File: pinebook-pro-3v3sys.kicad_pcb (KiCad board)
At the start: 2 copper layers, 7.8 x 17.9 mm, 23 parts, among them J1 Conn_01x03, J2 Conn_02x03_Counter_Clockwise, J3 Conn_01x01, J4 Conn_01x03, J5 Conn_01x01, U1 TPS63806

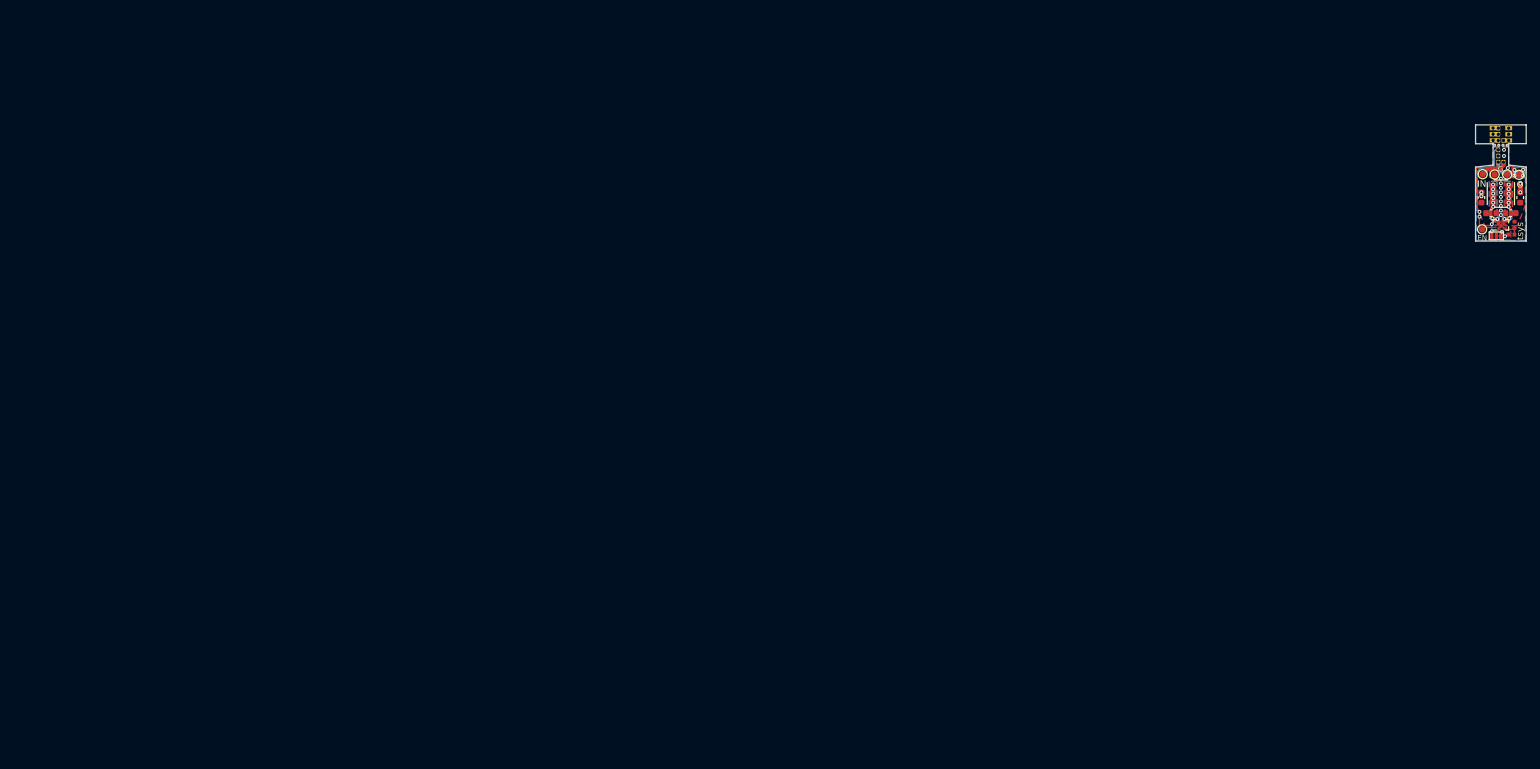
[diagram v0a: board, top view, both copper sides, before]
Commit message: Add manually panelized boards
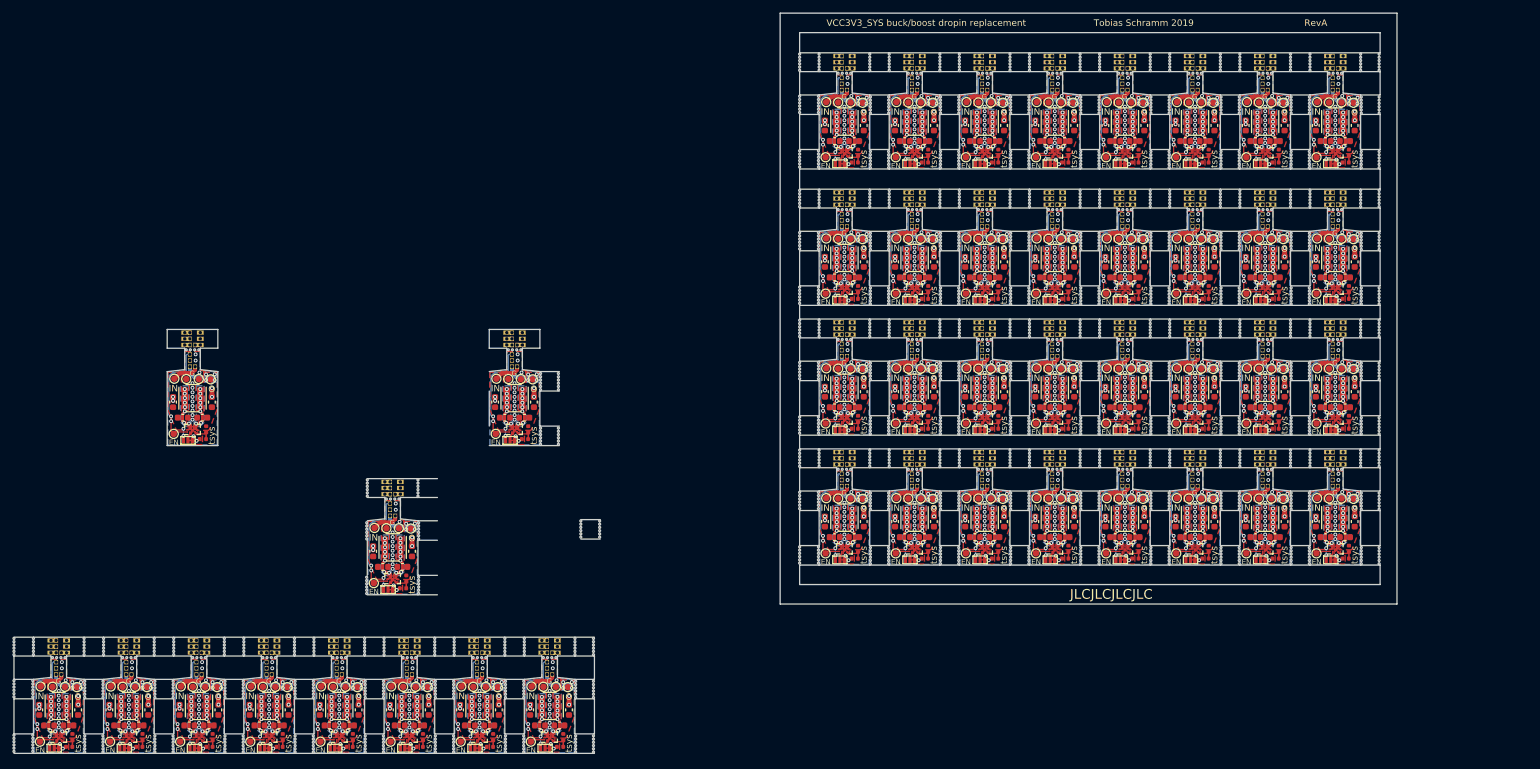
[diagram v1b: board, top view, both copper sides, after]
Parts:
- added C1: 22 uC, Capacitor_SMD:C_0603_1608Metric, F.Cu at (-42.7, 111.9)
- added C1: 22 uC, Capacitor_SMD:C_0603_1608Metric, F.Cu at (-61.7, 136.3)
- added C1: 22 uC, Capacitor_SMD:C_0603_1608Metric, F.Cu at (-29.3, 136.3)
- added C1: 22 uC, Capacitor_SMD:C_0603_1608Metric, F.Cu at (48.5, 46.3)
- added C1: 22 uC, Capacitor_SMD:C_0603_1608Metric, F.Cu at (102.5, 46.3)
- added C1: 22 uC, Capacitor_SMD:C_0603_1608Metric, F.Cu at (59.3, 46.3)
- added C1: 22 uC, Capacitor_SMD:C_0603_1608Metric, F.Cu at (91.7, 46.3)
- added C1: 22 uC, Capacitor_SMD:C_0603_1608Metric, F.Cu at (70.1, 46.3)
- added C1: 22 uC, Capacitor_SMD:C_0603_1608Metric, F.Cu at (80.9, 46.3)
- added C1: 22 uC, Capacitor_SMD:C_0603_1608Metric, F.Cu at (26.9, 46.3)
- added C1: 22 uC, Capacitor_SMD:C_0603_1608Metric, F.Cu at (37.7, 46.3)
- added C1: 22 uC, Capacitor_SMD:C_0603_1608Metric, F.Cu at (-23.9, 88.9)
- added C1: 22 uC, Capacitor_SMD:C_0603_1608Metric, F.Cu at (48.5, 67.3)
- added C1: 22 uC, Capacitor_SMD:C_0603_1608Metric, F.Cu at (102.5, 67.3)
- added C1: 22 uC, Capacitor_SMD:C_0603_1608Metric, F.Cu at (59.3, 67.3)
- added C1: 22 uC, Capacitor_SMD:C_0603_1608Metric, F.Cu at (91.7, 67.3)
- added C1: 22 uC, Capacitor_SMD:C_0603_1608Metric, F.Cu at (70.1, 67.3)
- added C1: 22 uC, Capacitor_SMD:C_0603_1608Metric, F.Cu at (80.9, 67.3)
- added C1: 22 uC, Capacitor_SMD:C_0603_1608Metric, F.Cu at (26.9, 67.3)
- added C1: 22 uC, Capacitor_SMD:C_0603_1608Metric, F.Cu at (37.7, 67.3)
- added C1: 22 uC, Capacitor_SMD:C_0603_1608Metric, F.Cu at (48.5, 87.3)
- added C1: 22 uC, Capacitor_SMD:C_0603_1608Metric, F.Cu at (102.5, 87.3)
- added C1: 22 uC, Capacitor_SMD:C_0603_1608Metric, F.Cu at (59.3, 87.3)
- added C1: 22 uC, Capacitor_SMD:C_0603_1608Metric, F.Cu at (91.7, 87.3)
- added C1: 22 uC, Capacitor_SMD:C_0603_1608Metric, F.Cu at (70.1, 87.3)
- added C1: 22 uC, Capacitor_SMD:C_0603_1608Metric, F.Cu at (80.9, 87.3)
- added C1: 22 uC, Capacitor_SMD:C_0603_1608Metric, F.Cu at (26.9, 87.3)
- added C1: 22 uC, Capacitor_SMD:C_0603_1608Metric, F.Cu at (37.7, 87.3)
- added C1: 22 uC, Capacitor_SMD:C_0603_1608Metric, F.Cu at (102.5, 107.3)
- added C1: 22 uC, Capacitor_SMD:C_0603_1608Metric, F.Cu at (91.7, 107.3)
- added C1: 22 uC, Capacitor_SMD:C_0603_1608Metric, F.Cu at (80.9, 107.3)
- added C1: 22 uC, Capacitor_SMD:C_0603_1608Metric, F.Cu at (70.1, 107.3)
- added C1: 22 uC, Capacitor_SMD:C_0603_1608Metric, F.Cu at (-40.1, 136.3)
- added C1: 22 uC, Capacitor_SMD:C_0603_1608Metric, F.Cu at (59.3, 107.3)
- added C1: 22 uC, Capacitor_SMD:C_0603_1608Metric, F.Cu at (48.5, 107.3)
- added C1: 22 uC, Capacitor_SMD:C_0603_1608Metric, F.Cu at (37.7, 107.3)
- added C1: 22 uC, Capacitor_SMD:C_0603_1608Metric, F.Cu at (26.9, 107.3)
- added C1: 22 uC, Capacitor_SMD:C_0603_1608Metric, F.Cu at (-94.1, 136.3)
- added C1: 22 uC, Capacitor_SMD:C_0603_1608Metric, F.Cu at (-50.9, 136.3)
- added C1: 22 uC, Capacitor_SMD:C_0603_1608Metric, F.Cu at (-18.5, 136.3)
- added C1: 22 uC, Capacitor_SMD:C_0603_1608Metric, F.Cu at (-83.3, 136.3)
- added C1: 22 uC, Capacitor_SMD:C_0603_1608Metric, F.Cu at (-72.5, 136.3)
- added C2: 22 uC, Capacitor_SMD:C_0603_1608Metric, F.Cu at (-17.0, 138.7)
- added C2: 22 uC, Capacitor_SMD:C_0603_1608Metric, F.Cu at (-49.4, 138.7)
- added C2: 22 uC, Capacitor_SMD:C_0603_1608Metric, F.Cu at (104.0, 48.7)
- added C2: 22 uC, Capacitor_SMD:C_0603_1608Metric, F.Cu at (71.6, 48.7)
- added C2: 22 uC, Capacitor_SMD:C_0603_1608Metric, F.Cu at (39.2, 48.7)
- added C2: 22 uC, Capacitor_SMD:C_0603_1608Metric, F.Cu at (28.4, 48.7)
- added C2: 22 uC, Capacitor_SMD:C_0603_1608Metric, F.Cu at (60.8, 48.7)
- added C2: 22 uC, Capacitor_SMD:C_0603_1608Metric, F.Cu at (50.0, 48.7)
- added C2: 22 uC, Capacitor_SMD:C_0603_1608Metric, F.Cu at (82.4, 48.7)
- added C2: 22 uC, Capacitor_SMD:C_0603_1608Metric, F.Cu at (93.2, 48.7)
- added C2: 22 uC, Capacitor_SMD:C_0603_1608Metric, F.Cu at (-22.4, 91.3)
- added C2: 22 uC, Capacitor_SMD:C_0603_1608Metric, F.Cu at (104.0, 69.7)
- added C2: 22 uC, Capacitor_SMD:C_0603_1608Metric, F.Cu at (71.6, 69.7)
- added C2: 22 uC, Capacitor_SMD:C_0603_1608Metric, F.Cu at (39.2, 69.7)
- added C2: 22 uC, Capacitor_SMD:C_0603_1608Metric, F.Cu at (28.4, 69.7)
- added C2: 22 uC, Capacitor_SMD:C_0603_1608Metric, F.Cu at (60.8, 69.7)
- added C2: 22 uC, Capacitor_SMD:C_0603_1608Metric, F.Cu at (50.0, 69.7)
- added C2: 22 uC, Capacitor_SMD:C_0603_1608Metric, F.Cu at (82.4, 69.7)
- added C2: 22 uC, Capacitor_SMD:C_0603_1608Metric, F.Cu at (93.2, 69.7)
- added C2: 22 uC, Capacitor_SMD:C_0603_1608Metric, F.Cu at (104.0, 89.7)
- added C2: 22 uC, Capacitor_SMD:C_0603_1608Metric, F.Cu at (71.6, 89.7)
- added C2: 22 uC, Capacitor_SMD:C_0603_1608Metric, F.Cu at (-41.2, 114.3)
- added C2: 22 uC, Capacitor_SMD:C_0603_1608Metric, F.Cu at (39.2, 89.7)
- added C2: 22 uC, Capacitor_SMD:C_0603_1608Metric, F.Cu at (28.4, 89.7)
- added C2: 22 uC, Capacitor_SMD:C_0603_1608Metric, F.Cu at (60.8, 89.7)
- added C2: 22 uC, Capacitor_SMD:C_0603_1608Metric, F.Cu at (50.0, 89.7)
- added C2: 22 uC, Capacitor_SMD:C_0603_1608Metric, F.Cu at (82.4, 89.7)
- added C2: 22 uC, Capacitor_SMD:C_0603_1608Metric, F.Cu at (93.2, 89.7)
- added C2: 22 uC, Capacitor_SMD:C_0603_1608Metric, F.Cu at (104.0, 109.7)
- added C2: 22 uC, Capacitor_SMD:C_0603_1608Metric, F.Cu at (93.2, 109.7)
- added C2: 22 uC, Capacitor_SMD:C_0603_1608Metric, F.Cu at (82.4, 109.7)
- added C2: 22 uC, Capacitor_SMD:C_0603_1608Metric, F.Cu at (71.6, 109.7)
- added C2: 22 uC, Capacitor_SMD:C_0603_1608Metric, F.Cu at (-92.6, 138.7)
- added C2: 22 uC, Capacitor_SMD:C_0603_1608Metric, F.Cu at (60.8, 109.7)
- added C2: 22 uC, Capacitor_SMD:C_0603_1608Metric, F.Cu at (50.0, 109.7)
- added C2: 22 uC, Capacitor_SMD:C_0603_1608Metric, F.Cu at (39.2, 109.7)
- added C2: 22 uC, Capacitor_SMD:C_0603_1608Metric, F.Cu at (28.4, 109.7)
- added C2: 22 uC, Capacitor_SMD:C_0603_1608Metric, F.Cu at (-81.8, 138.7)
- added C2: 22 uC, Capacitor_SMD:C_0603_1608Metric, F.Cu at (-27.8, 138.7)
- added C2: 22 uC, Capacitor_SMD:C_0603_1608Metric, F.Cu at (-60.2, 138.7)
- added C2: 22 uC, Capacitor_SMD:C_0603_1608Metric, F.Cu at (-71.0, 138.7)
- added C2: 22 uC, Capacitor_SMD:C_0603_1608Metric, F.Cu at (-38.6, 138.7)
- added C3: 22 uC, Capacitor_SMD:C_0603_1608Metric, F.Cu at (-17.9, 88.9)
- added C3: 22 uC, Capacitor_SMD:C_0603_1608Metric, F.Cu at (-12.5, 136.3)
- added C3: 22 uC, Capacitor_SMD:C_0603_1608Metric, F.Cu at (-55.7, 136.3)
- added C3: 22 uC, Capacitor_SMD:C_0603_1608Metric, F.Cu at (65.3, 46.3)
- added C3: 22 uC, Capacitor_SMD:C_0603_1608Metric, F.Cu at (97.7, 46.3)
- added C3: 22 uC, Capacitor_SMD:C_0603_1608Metric, F.Cu at (76.1, 46.3)
- added C3: 22 uC, Capacitor_SMD:C_0603_1608Metric, F.Cu at (54.5, 46.3)
- added C3: 22 uC, Capacitor_SMD:C_0603_1608Metric, F.Cu at (108.5, 46.3)
- added C3: 22 uC, Capacitor_SMD:C_0603_1608Metric, F.Cu at (86.9, 46.3)
- added C3: 22 uC, Capacitor_SMD:C_0603_1608Metric, F.Cu at (32.9, 46.3)
- added C3: 22 uC, Capacitor_SMD:C_0603_1608Metric, F.Cu at (43.7, 46.3)
- added C3: 22 uC, Capacitor_SMD:C_0603_1608Metric, F.Cu at (65.3, 67.3)
- added C3: 22 uC, Capacitor_SMD:C_0603_1608Metric, F.Cu at (97.7, 67.3)
- added C3: 22 uC, Capacitor_SMD:C_0603_1608Metric, F.Cu at (76.1, 67.3)
- added C3: 22 uC, Capacitor_SMD:C_0603_1608Metric, F.Cu at (54.5, 67.3)
- added C3: 22 uC, Capacitor_SMD:C_0603_1608Metric, F.Cu at (108.5, 67.3)
- added C3: 22 uC, Capacitor_SMD:C_0603_1608Metric, F.Cu at (86.9, 67.3)
- added C3: 22 uC, Capacitor_SMD:C_0603_1608Metric, F.Cu at (32.9, 67.3)
- added C3: 22 uC, Capacitor_SMD:C_0603_1608Metric, F.Cu at (43.7, 67.3)
- added C3: 22 uC, Capacitor_SMD:C_0603_1608Metric, F.Cu at (65.3, 87.3)
- added C3: 22 uC, Capacitor_SMD:C_0603_1608Metric, F.Cu at (97.7, 87.3)
- added C3: 22 uC, Capacitor_SMD:C_0603_1608Metric, F.Cu at (-36.7, 111.9)
- added C3: 22 uC, Capacitor_SMD:C_0603_1608Metric, F.Cu at (76.1, 87.3)
- added C3: 22 uC, Capacitor_SMD:C_0603_1608Metric, F.Cu at (54.5, 87.3)
- added C3: 22 uC, Capacitor_SMD:C_0603_1608Metric, F.Cu at (108.5, 87.3)
- added C3: 22 uC, Capacitor_SMD:C_0603_1608Metric, F.Cu at (86.9, 87.3)
- added C3: 22 uC, Capacitor_SMD:C_0603_1608Metric, F.Cu at (32.9, 87.3)
- added C3: 22 uC, Capacitor_SMD:C_0603_1608Metric, F.Cu at (43.7, 87.3)
- added C3: 22 uC, Capacitor_SMD:C_0603_1608Metric, F.Cu at (108.5, 107.3)
- added C3: 22 uC, Capacitor_SMD:C_0603_1608Metric, F.Cu at (97.7, 107.3)
- added C3: 22 uC, Capacitor_SMD:C_0603_1608Metric, F.Cu at (86.9, 107.3)
- added C3: 22 uC, Capacitor_SMD:C_0603_1608Metric, F.Cu at (76.1, 107.3)
- added C3: 22 uC, Capacitor_SMD:C_0603_1608Metric, F.Cu at (-34.1, 136.3)
- added C3: 22 uC, Capacitor_SMD:C_0603_1608Metric, F.Cu at (65.3, 107.3)
- added C3: 22 uC, Capacitor_SMD:C_0603_1608Metric, F.Cu at (54.5, 107.3)
- added C3: 22 uC, Capacitor_SMD:C_0603_1608Metric, F.Cu at (43.7, 107.3)
- added C3: 22 uC, Capacitor_SMD:C_0603_1608Metric, F.Cu at (32.9, 107.3)
- added C3: 22 uC, Capacitor_SMD:C_0603_1608Metric, F.Cu at (-88.1, 136.3)
- added C3: 22 uC, Capacitor_SMD:C_0603_1608Metric, F.Cu at (-66.5, 136.3)
- added C3: 22 uC, Capacitor_SMD:C_0603_1608Metric, F.Cu at (-77.3, 136.3)
- added C3: 22 uC, Capacitor_SMD:C_0603_1608Metric, F.Cu at (-23.3, 136.3)
- added C3: 22 uC, Capacitor_SMD:C_0603_1608Metric, F.Cu at (-44.9, 136.3)
- added C4: 22 uC, Capacitor_SMD:C_0603_1608Metric, F.Cu at (-19.4, 91.3)
- added C4: 22 uC, Capacitor_SMD:C_0603_1608Metric, F.Cu at (-68.0, 138.7)
- added C4: 22 uC, Capacitor_SMD:C_0603_1608Metric, F.Cu at (-14.0, 138.7)
- added C4: 22 uC, Capacitor_SMD:C_0603_1608Metric, F.Cu at (107.0, 48.7)
- added C4: 22 uC, Capacitor_SMD:C_0603_1608Metric, F.Cu at (53.0, 48.7)
- added C4: 22 uC, Capacitor_SMD:C_0603_1608Metric, F.Cu at (63.8, 48.7)
- added C4: 22 uC, Capacitor_SMD:C_0603_1608Metric, F.Cu at (42.2, 48.7)
- added C4: 22 uC, Capacitor_SMD:C_0603_1608Metric, F.Cu at (85.4, 48.7)
- added C4: 22 uC, Capacitor_SMD:C_0603_1608Metric, F.Cu at (74.6, 48.7)
- added C4: 22 uC, Capacitor_SMD:C_0603_1608Metric, F.Cu at (96.2, 48.7)
- added C4: 22 uC, Capacitor_SMD:C_0603_1608Metric, F.Cu at (31.4, 48.7)
- added C4: 22 uC, Capacitor_SMD:C_0603_1608Metric, F.Cu at (107.0, 69.7)
- added C4: 22 uC, Capacitor_SMD:C_0603_1608Metric, F.Cu at (53.0, 69.7)
- added C4: 22 uC, Capacitor_SMD:C_0603_1608Metric, F.Cu at (63.8, 69.7)
- added C4: 22 uC, Capacitor_SMD:C_0603_1608Metric, F.Cu at (42.2, 69.7)
- added C4: 22 uC, Capacitor_SMD:C_0603_1608Metric, F.Cu at (85.4, 69.7)
- added C4: 22 uC, Capacitor_SMD:C_0603_1608Metric, F.Cu at (74.6, 69.7)
- added C4: 22 uC, Capacitor_SMD:C_0603_1608Metric, F.Cu at (96.2, 69.7)
- added C4: 22 uC, Capacitor_SMD:C_0603_1608Metric, F.Cu at (31.4, 69.7)
- added C4: 22 uC, Capacitor_SMD:C_0603_1608Metric, F.Cu at (107.0, 89.7)
- added C4: 22 uC, Capacitor_SMD:C_0603_1608Metric, F.Cu at (53.0, 89.7)
- added C4: 22 uC, Capacitor_SMD:C_0603_1608Metric, F.Cu at (-38.2, 114.3)
- added C4: 22 uC, Capacitor_SMD:C_0603_1608Metric, F.Cu at (63.8, 89.7)
- added C4: 22 uC, Capacitor_SMD:C_0603_1608Metric, F.Cu at (42.2, 89.7)
- added C4: 22 uC, Capacitor_SMD:C_0603_1608Metric, F.Cu at (85.4, 89.7)
- added C4: 22 uC, Capacitor_SMD:C_0603_1608Metric, F.Cu at (74.6, 89.7)
- added C4: 22 uC, Capacitor_SMD:C_0603_1608Metric, F.Cu at (96.2, 89.7)
- added C4: 22 uC, Capacitor_SMD:C_0603_1608Metric, F.Cu at (31.4, 89.7)
- added C4: 22 uC, Capacitor_SMD:C_0603_1608Metric, F.Cu at (107.0, 109.7)
- added C4: 22 uC, Capacitor_SMD:C_0603_1608Metric, F.Cu at (96.2, 109.7)
- added C4: 22 uC, Capacitor_SMD:C_0603_1608Metric, F.Cu at (85.4, 109.7)
- added C4: 22 uC, Capacitor_SMD:C_0603_1608Metric, F.Cu at (74.6, 109.7)
- added C4: 22 uC, Capacitor_SMD:C_0603_1608Metric, F.Cu at (-35.6, 138.7)
- added C4: 22 uC, Capacitor_SMD:C_0603_1608Metric, F.Cu at (63.8, 109.7)
- added C4: 22 uC, Capacitor_SMD:C_0603_1608Metric, F.Cu at (53.0, 109.7)
- added C4: 22 uC, Capacitor_SMD:C_0603_1608Metric, F.Cu at (42.2, 109.7)
- added C4: 22 uC, Capacitor_SMD:C_0603_1608Metric, F.Cu at (31.4, 109.7)
- added C4: 22 uC, Capacitor_SMD:C_0603_1608Metric, F.Cu at (-24.8, 138.7)
- added C4: 22 uC, Capacitor_SMD:C_0603_1608Metric, F.Cu at (-78.8, 138.7)
- added C4: 22 uC, Capacitor_SMD:C_0603_1608Metric, F.Cu at (-46.4, 138.7)
- added C4: 22 uC, Capacitor_SMD:C_0603_1608Metric, F.Cu at (-89.6, 138.7)
- added C4: 22 uC, Capacitor_SMD:C_0603_1608Metric, F.Cu at (-57.2, 138.7)
- added H1: MountingHole, Mousebite:Mousebite_0.3mm, F.Cu at (-14.2, 86.5)
- added H1: MountingHole, Mousebite:Mousebite_0.3mm, F.Cu at (-7.80, 108.7)
- added H1: MountingHole, Mousebite:Mousebite_0.3mm, F.Cu at (-22.3, 133.4)
- added H1: MountingHole, Mousebite:Mousebite_0.3mm, F.Cu at (98.6, 56.8)
- added H1: MountingHole, Mousebite:Mousebite_0.3mm, F.Cu at (98.7, 63.9)
- added H1: MountingHole, Mousebite:Mousebite_0.3mm, F.Cu at (90.8, 56.3)
- added H1: MountingHole, Mousebite:Mousebite_0.3mm, F.Cu at (90.8, 56.8)
- added H1: MountingHole, Mousebite:Mousebite_0.3mm, F.Cu at (98.6, 57.8)
- added H1: MountingHole, Mousebite:Mousebite_0.3mm, F.Cu at (98.6, 58.8)
- added H1: MountingHole, Mousebite:Mousebite_0.3mm, F.Cu at (90.7, 63.9)
- added H1: MountingHole, Mousebite:Mousebite_0.3mm, F.Cu at (98.7, 73.8)
- added H1: MountingHole, Mousebite:Mousebite_0.3mm, F.Cu at (98.7, 72.8)
- added H1: MountingHole, Mousebite:Mousebite_0.3mm, F.Cu at (98.7, 71.3)
- added H1: MountingHole, Mousebite:Mousebite_0.3mm, F.Cu at (-22.3, 140.3)
- added H1: MountingHole, Mousebite:Mousebite_0.3mm, F.Cu at (98.7, 64.4)
- added H1: MountingHole, Mousebite:Mousebite_0.3mm, F.Cu at (90.7, 62.9)
- added H1: MountingHole, Mousebite:Mousebite_0.3mm, F.Cu at (90.7, 63.4)
- added H1: MountingHole, Mousebite:Mousebite_0.3mm, F.Cu at (90.7, 71.8)
- added H1: MountingHole, Mousebite:Mousebite_0.3mm, F.Cu at (98.7, 64.9)
- added H1: MountingHole, Mousebite:Mousebite_0.3mm, F.Cu at (90.7, 65.4)
- added H1: MountingHole, Mousebite:Mousebite_0.3mm, F.Cu at (90.7, 73.8)
- added H1: MountingHole, Mousebite:Mousebite_0.3mm, F.Cu at (33.8, 58.3)
- added H1: MountingHole, Mousebite:Mousebite_0.3mm, F.Cu at (101.5, 63.4)
- added H1: MountingHole, Mousebite:Mousebite_0.3mm, F.Cu at (101.5, 71.8)
- added H1: MountingHole, Mousebite:Mousebite_0.3mm, F.Cu at (-87.1, 142.3)
- added H1: MountingHole, Mousebite:Mousebite_0.3mm, F.Cu at (101.5, 72.3)
- added H1: MountingHole, Mousebite:Mousebite_0.3mm, F.Cu at (23.0, 57.8)
- added H1: MountingHole, Mousebite:Mousebite_0.3mm, F.Cu at (23.0, 56.8)
- added H1: MountingHole, Mousebite:Mousebite_0.3mm, F.Cu at (23.0, 57.3)
- added H1: MountingHole, Mousebite:Mousebite_0.3mm, F.Cu at (55.5, 73.8)
- added H1: MountingHole, Mousebite:Mousebite_0.3mm, F.Cu at (23.0, 58.8)
- added H1: MountingHole, Mousebite:Mousebite_0.3mm, F.Cu at (101.6, 57.3)
- added H1: MountingHole, Mousebite:Mousebite_0.3mm, F.Cu at (66.3, 64.4)
- added H1: MountingHole, Mousebite:Mousebite_0.3mm, F.Cu at (69.1, 72.3)
- added H1: MountingHole, Mousebite:Mousebite_0.3mm, F.Cu at (69.1, 64.4)
- added H1: MountingHole, Mousebite:Mousebite_0.3mm, F.Cu at (-92.1, 128.2)
- added H1: MountingHole, Mousebite:Mousebite_0.3mm, F.Cu at (69.1, 64.9)
- added H1: MountingHole, Mousebite:Mousebite_0.3mm, F.Cu at (77.1, 71.8)
- added H1: MountingHole, Mousebite:Mousebite_0.3mm, F.Cu at (55.5, 72.3)
- added H1: MountingHole, Mousebite:Mousebite_0.3mm, F.Cu at (69.2, 58.8)
- added H1: MountingHole, Mousebite:Mousebite_0.3mm, F.Cu at (69.2, 58.3)
- added H1: MountingHole, Mousebite:Mousebite_0.3mm, F.Cu at (101.5, 73.3)
- added H1: MountingHole, Mousebite:Mousebite_0.3mm, F.Cu at (47.6, 58.3)
- added H1: MountingHole, Mousebite:Mousebite_0.3mm, F.Cu at (25.9, 71.2)
- added H1: MountingHole, Mousebite:Mousebite_0.3mm, F.Cu at (33.9, 64.9)
- added H1: MountingHole, Mousebite:Mousebite_0.3mm, F.Cu at (23.0, 64.8)
- added H1: MountingHole, Mousebite:Mousebite_0.3mm, F.Cu at (-87.1, 141.8)
- added H1: MountingHole, Mousebite:Mousebite_0.3mm, F.Cu at (36.7, 73.3)
- added H1: MountingHole, Mousebite:Mousebite_0.3mm, F.Cu at (44.7, 63.4)
- added H1: MountingHole, Mousebite:Mousebite_0.3mm, F.Cu at (25.9, 64.8)
- added H1: MountingHole, Mousebite:Mousebite_0.3mm, F.Cu at (36.7, 64.9)
- added H1: MountingHole, Mousebite:Mousebite_0.3mm, F.Cu at (44.7, 71.8)
- added H1: MountingHole, Mousebite:Mousebite_0.3mm, F.Cu at (66.3, 63.9)
- added H1: MountingHole, Mousebite:Mousebite_0.3mm, F.Cu at (55.5, 72.8)
- added H1: MountingHole, Mousebite:Mousebite_0.3mm, F.Cu at (79.9, 71.3)
- added H1: MountingHole, Mousebite:Mousebite_0.3mm, F.Cu at (55.5, 63.9)
- added H1: MountingHole, Mousebite:Mousebite_0.3mm, F.Cu at (55.4, 56.8)
- added H1: MountingHole, Mousebite:Mousebite_0.3mm, F.Cu at (-84.3, 142.8)
- added H1: MountingHole, Mousebite:Mousebite_0.3mm, F.Cu at (44.7, 73.3)
- added H1: MountingHole, Mousebite:Mousebite_0.3mm, F.Cu at (39.7, 59.2)
- added H1: MountingHole, Mousebite:Mousebite_0.3mm, F.Cu at (23.0, 62.8)
- added H1: MountingHole, Mousebite:Mousebite_0.3mm, F.Cu at (23.0, 64.3)
- added H1: MountingHole, Mousebite:Mousebite_0.3mm, F.Cu at (79.9, 63.9)
- added H1: MountingHole, Mousebite:Mousebite_0.3mm, F.Cu at (87.9, 73.8)
- added H1: MountingHole, Mousebite:Mousebite_0.3mm, F.Cu at (47.5, 73.8)
- added H1: MountingHole, Mousebite:Mousebite_0.3mm, F.Cu at (44.7, 62.9)
- added H1: MountingHole, Mousebite:Mousebite_0.3mm, F.Cu at (44.7, 72.3)
- added H1: MountingHole, Mousebite:Mousebite_0.3mm, F.Cu at (36.7, 72.8)
- added H1: MountingHole, Mousebite:Mousebite_0.3mm, F.Cu at (-87.1, 134.4)
- added H1: MountingHole, Mousebite:Mousebite_0.3mm, F.Cu at (33.9, 63.9)
- added H1: MountingHole, Mousebite:Mousebite_0.3mm, F.Cu at (25.9, 73.7)
- added H1: MountingHole, Mousebite:Mousebite_0.3mm, F.Cu at (33.9, 73.8)
- added H1: MountingHole, Mousebite:Mousebite_0.3mm, F.Cu at (25.9, 73.2)
- added H1: MountingHole, Mousebite:Mousebite_0.3mm, F.Cu at (33.9, 71.8)
- added H1: MountingHole, Mousebite:Mousebite_0.3mm, F.Cu at (25.9, 63.8)
- added H1: MountingHole, Mousebite:Mousebite_0.3mm, F.Cu at (25.9, 62.8)
- added H1: MountingHole, Mousebite:Mousebite_0.3mm, F.Cu at (47.5, 65.4)
- added H1: MountingHole, Mousebite:Mousebite_0.3mm, F.Cu at (55.4, 58.3)
- added H1: MountingHole, Mousebite:Mousebite_0.3mm, F.Cu at (58.3, 72.3)
- added H1: MountingHole, Mousebite:Mousebite_0.3mm, F.Cu at (-98.0, 140.7)
- added H1: MountingHole, Mousebite:Mousebite_0.3mm, F.Cu at (47.6, 58.8)
- added H1: MountingHole, Mousebite:Mousebite_0.3mm, F.Cu at (61.3, 59.2)
- added H1: MountingHole, Mousebite:Mousebite_0.3mm, F.Cu at (44.6, 78.3)
- added H1: MountingHole, Mousebite:Mousebite_0.3mm, F.Cu at (44.6, 76.3)
- added H1: MountingHole, Mousebite:Mousebite_0.3mm, F.Cu at (44.6, 76.8)
- added H1: MountingHole, Mousebite:Mousebite_0.3mm, F.Cu at (112.2, 76.8)
- added H1: MountingHole, Mousebite:Mousebite_0.3mm, F.Cu at (112.2, 78.3)
- added H1: MountingHole, Mousebite:Mousebite_0.3mm, F.Cu at (112.2, 76.3)
- added H1: MountingHole, Mousebite:Mousebite_0.3mm, F.Cu at (101.5, 93.8)
- added H1: MountingHole, Mousebite:Mousebite_0.3mm, F.Cu at (101.5, 85.4)
- added H1: MountingHole, Mousebite:Mousebite_0.3mm, F.Cu at (-87.1, 132.4)
- added H1: MountingHole, Mousebite:Mousebite_0.3mm, F.Cu at (109.5, 85.4)
- added H1: MountingHole, Mousebite:Mousebite_0.3mm, F.Cu at (109.5, 83.4)
- added H1: MountingHole, Mousebite:Mousebite_0.3mm, F.Cu at (109.5, 82.9)
- added H1: MountingHole, Mousebite:Mousebite_0.3mm, F.Cu at (101.6, 78.8)
- added H1: MountingHole, Mousebite:Mousebite_0.3mm, F.Cu at (109.5, 93.3)
- added H1: MountingHole, Mousebite:Mousebite_0.3mm, F.Cu at (112.2, 78.8)
- added H1: MountingHole, Mousebite:Mousebite_0.3mm, F.Cu at (112.2, 77.3)
- added H1: MountingHole, Mousebite:Mousebite_0.3mm, F.Cu at (112.2, 77.8)
- added H1: MountingHole, Mousebite:Mousebite_0.3mm, F.Cu at (109.4, 77.3)
- added H1: MountingHole, Mousebite:Mousebite_0.3mm, F.Cu at (98.7, 92.3)
- added H1: MountingHole, Mousebite:Mousebite_0.3mm, F.Cu at (-84.3, 134.4)
- added H1: MountingHole, Mousebite:Mousebite_0.3mm, F.Cu at (79.9, 84.9)
- added H1: MountingHole, Mousebite:Mousebite_0.3mm, F.Cu at (87.9, 91.8)
- added H1: MountingHole, Mousebite:Mousebite_0.3mm, F.Cu at (80.0, 76.3)
- added H1: MountingHole, Mousebite:Mousebite_0.3mm, F.Cu at (80.0, 76.8)
- added H1: MountingHole, Mousebite:Mousebite_0.3mm, F.Cu at (87.8, 77.8)
- added H1: MountingHole, Mousebite:Mousebite_0.3mm, F.Cu at (87.8, 78.8)
- added H1: MountingHole, Mousebite:Mousebite_0.3mm, F.Cu at (98.7, 82.9)
- added H1: MountingHole, Mousebite:Mousebite_0.3mm, F.Cu at (90.7, 92.8)
- added H1: MountingHole, Mousebite:Mousebite_0.3mm, F.Cu at (104.5, 79.2)
- added H1: MountingHole, Mousebite:Mousebite_0.3mm, F.Cu at (109.5, 84.9)
- added H1: MountingHole, Mousebite:Mousebite_0.3mm, F.Cu at (-14.2, 86.0)
- added H1: MountingHole, Mousebite:Mousebite_0.3mm, F.Cu at (-98.0, 133.8)
- added H1: MountingHole, Mousebite:Mousebite_0.3mm, F.Cu at (101.5, 91.3)
- added H1: MountingHole, Mousebite:Mousebite_0.3mm, F.Cu at (101.5, 83.9)
- added H1: MountingHole, Mousebite:Mousebite_0.3mm, F.Cu at (101.5, 84.4)
- added H1: MountingHole, Mousebite:Mousebite_0.3mm, F.Cu at (69.1, 83.9)
- added H1: MountingHole, Mousebite:Mousebite_0.3mm, F.Cu at (77.1, 93.8)
- added H1: MountingHole, Mousebite:Mousebite_0.3mm, F.Cu at (77.1, 92.8)
- added H1: MountingHole, Mousebite:Mousebite_0.3mm, F.Cu at (66.2, 76.8)
- added H1: MountingHole, Mousebite:Mousebite_0.3mm, F.Cu at (58.3, 92.8)
- added H1: MountingHole, Mousebite:Mousebite_0.3mm, F.Cu at (112.2, 91.3)
- added H1: MountingHole, Mousebite:Mousebite_0.3mm, F.Cu at (47.5, 93.3)
- added H1: MountingHole, Mousebite:Mousebite_0.3mm, F.Cu at (-33.2, 126.3)
- added H1: MountingHole, Mousebite:Mousebite_0.3mm, F.Cu at (33.8, 77.8)
- added H1: MountingHole, Mousebite:Mousebite_0.3mm, F.Cu at (26.0, 78.8)
- added H1: MountingHole, Mousebite:Mousebite_0.3mm, F.Cu at (66.3, 82.9)
- added H1: MountingHole, Mousebite:Mousebite_0.3mm, F.Cu at (66.2, 78.3)
- added H1: MountingHole, Mousebite:Mousebite_0.3mm, F.Cu at (47.6, 76.3)
- added H1: MountingHole, Mousebite:Mousebite_0.3mm, F.Cu at (47.5, 83.9)
- added H1: MountingHole, Mousebite:Mousebite_0.3mm, F.Cu at (101.5, 92.8)
- added H1: MountingHole, Mousebite:Mousebite_0.3mm, F.Cu at (109.5, 91.8)
- added H1: MountingHole, Mousebite:Mousebite_0.3mm, F.Cu at (87.9, 91.3)
- added H1: MountingHole, Mousebite:Mousebite_0.3mm, F.Cu at (87.9, 84.4)
- added H1: MountingHole, Mousebite:Mousebite_0.3mm, F.Cu at (-41.0, 126.8)
- added H1: MountingHole, Mousebite:Mousebite_0.3mm, F.Cu at (79.9, 82.9)
- added H1: MountingHole, Mousebite:Mousebite_0.3mm, F.Cu at (79.9, 83.4)
- added H1: MountingHole, Mousebite:Mousebite_0.3mm, F.Cu at (79.9, 91.8)
- added H1: MountingHole, Mousebite:Mousebite_0.3mm, F.Cu at (66.2, 77.3)
- added H1: MountingHole, Mousebite:Mousebite_0.3mm, F.Cu at (58.3, 83.4)
- added H1: MountingHole, Mousebite:Mousebite_0.3mm, F.Cu at (58.3, 82.9)
- added H1: MountingHole, Mousebite:Mousebite_0.3mm, F.Cu at (58.4, 76.8)
- added H1: MountingHole, Mousebite:Mousebite_0.3mm, F.Cu at (58.3, 91.3)
- added H1: MountingHole, Mousebite:Mousebite_0.3mm, F.Cu at (66.3, 92.3)
- added H1: MountingHole, Mousebite:Mousebite_0.3mm, F.Cu at (55.4, 76.3)
- added H1: MountingHole, Mousebite:Mousebite_0.3mm, F.Cu at (-41.0, 126.3)
- added H1: MountingHole, Mousebite:Mousebite_0.3mm, F.Cu at (44.7, 83.9)
- added H1: MountingHole, Mousebite:Mousebite_0.3mm, F.Cu at (66.2, 77.8)
- added H1: MountingHole, Mousebite:Mousebite_0.3mm, F.Cu at (58.3, 84.4)
- added H1: MountingHole, Mousebite:Mousebite_0.3mm, F.Cu at (23.0, 83.8)
- added H1: MountingHole, Mousebite:Mousebite_0.3mm, F.Cu at (109.4, 78.3)
- added H1: MountingHole, Mousebite:Mousebite_0.3mm, F.Cu at (109.4, 76.3)
- added H1: MountingHole, Mousebite:Mousebite_0.3mm, F.Cu at (109.4, 76.8)
- added H1: MountingHole, Mousebite:Mousebite_0.3mm, F.Cu at (109.5, 83.9)
- added H1: MountingHole, Mousebite:Mousebite_0.3mm, F.Cu at (101.6, 76.3)
- added H1: MountingHole, Mousebite:Mousebite_0.3mm, F.Cu at (101.6, 76.8)
- added H1: MountingHole, Mousebite:Mousebite_0.3mm, F.Cu at (-41.0, 127.3)
- added H1: MountingHole, Mousebite:Mousebite_0.3mm, F.Cu at (109.4, 77.8)
- added H1: MountingHole, Mousebite:Mousebite_0.3mm, F.Cu at (109.4, 78.8)
- added H1: MountingHole, Mousebite:Mousebite_0.3mm, F.Cu at (109.5, 93.8)
- added H1: MountingHole, Mousebite:Mousebite_0.3mm, F.Cu at (109.5, 92.8)
- added H1: MountingHole, Mousebite:Mousebite_0.3mm, F.Cu at (55.5, 84.4)
- added H1: MountingHole, Mousebite:Mousebite_0.3mm, F.Cu at (66.2, 76.3)
- added H1: MountingHole, Mousebite:Mousebite_0.3mm, F.Cu at (58.3, 93.3)
- added H1: MountingHole, Mousebite:Mousebite_0.3mm, F.Cu at (66.3, 91.8)
- added H1: MountingHole, Mousebite:Mousebite_0.3mm, F.Cu at (66.3, 93.3)
- added H1: MountingHole, Mousebite:Mousebite_0.3mm, F.Cu at (69.1, 93.8)
- added H1: MountingHole, Mousebite:Mousebite_0.3mm, F.Cu at (-41.0, 127.8)
- added H1: MountingHole, Mousebite:Mousebite_0.3mm, F.Cu at (77.1, 83.4)
- added H1: MountingHole, Mousebite:Mousebite_0.3mm, F.Cu at (87.9, 93.3)
- added H1: MountingHole, Mousebite:Mousebite_0.3mm, F.Cu at (82.9, 79.2)
- added H1: MountingHole, Mousebite:Mousebite_0.3mm, F.Cu at (47.5, 92.3)
- added H1: MountingHole, Mousebite:Mousebite_0.3mm, F.Cu at (58.3, 85.4)
- added H1: MountingHole, Mousebite:Mousebite_0.3mm, F.Cu at (47.5, 91.3)
- added H1: MountingHole, Mousebite:Mousebite_0.3mm, F.Cu at (47.5, 82.9)
- added H1: MountingHole, Mousebite:Mousebite_0.3mm, F.Cu at (58.3, 91.8)
- added H1: MountingHole, Mousebite:Mousebite_0.3mm, F.Cu at (112.2, 93.3)
- added H1: MountingHole, Mousebite:Mousebite_0.3mm, F.Cu at (58.4, 77.3)
- added H1: MountingHole, Mousebite:Mousebite_0.3mm, F.Cu at (-44.0, 127.8)
- added H1: MountingHole, Mousebite:Mousebite_0.3mm, F.Cu at (47.5, 91.8)
- added H1: MountingHole, Mousebite:Mousebite_0.3mm, F.Cu at (66.3, 93.8)
- added H1: MountingHole, Mousebite:Mousebite_0.3mm, F.Cu at (66.3, 91.3)
- added H1: MountingHole, Mousebite:Mousebite_0.3mm, F.Cu at (47.5, 84.4)
- added H1: MountingHole, Mousebite:Mousebite_0.3mm, F.Cu at (58.4, 77.8)
- added H1: MountingHole, Mousebite:Mousebite_0.3mm, F.Cu at (112.2, 82.9)
- added H1: MountingHole, Mousebite:Mousebite_0.3mm, F.Cu at (47.6, 77.8)
- added H1: MountingHole, Mousebite:Mousebite_0.3mm, F.Cu at (55.5, 82.9)
- added H1: MountingHole, Mousebite:Mousebite_0.3mm, F.Cu at (33.8, 78.8)
- added H1: MountingHole, Mousebite:Mousebite_0.3mm, F.Cu at (55.5, 93.3)
- added H1: MountingHole, Mousebite:Mousebite_0.3mm, F.Cu at (-54.7, 134.4)
- added H1: MountingHole, Mousebite:Mousebite_0.3mm, F.Cu at (36.8, 76.3)
- added H1: MountingHole, Mousebite:Mousebite_0.3mm, F.Cu at (77.1, 82.9)
- added H1: MountingHole, Mousebite:Mousebite_0.3mm, F.Cu at (36.8, 76.8)
- added H1: MountingHole, Mousebite:Mousebite_0.3mm, F.Cu at (77.0, 76.8)
- added H1: MountingHole, Mousebite:Mousebite_0.3mm, F.Cu at (77.1, 83.9)
- added H1: MountingHole, Mousebite:Mousebite_0.3mm, F.Cu at (69.2, 76.3)
- added H1: MountingHole, Mousebite:Mousebite_0.3mm, F.Cu at (69.2, 76.8)
- added H1: MountingHole, Mousebite:Mousebite_0.3mm, F.Cu at (77.0, 77.8)
- added H1: MountingHole, Mousebite:Mousebite_0.3mm, F.Cu at (87.9, 92.3)
- added H1: MountingHole, Mousebite:Mousebite_0.3mm, F.Cu at (87.8, 78.3)
- added H1: MountingHole, Mousebite:Mousebite_0.3mm, F.Cu at (-65.6, 126.3)
- added H1: MountingHole, Mousebite:Mousebite_0.3mm, F.Cu at (87.8, 76.3)
- added H1: MountingHole, Mousebite:Mousebite_0.3mm, F.Cu at (87.8, 76.8)
- added H1: MountingHole, Mousebite:Mousebite_0.3mm, F.Cu at (87.9, 83.9)
- added H1: MountingHole, Mousebite:Mousebite_0.3mm, F.Cu at (77.1, 93.3)
- added H1: MountingHole, Mousebite:Mousebite_0.3mm, F.Cu at (72.1, 79.2)
- added H1: MountingHole, Mousebite:Mousebite_0.3mm, F.Cu at (69.1, 91.3)
- added H1: MountingHole, Mousebite:Mousebite_0.3mm, F.Cu at (55.5, 91.8)
- added H1: MountingHole, Mousebite:Mousebite_0.3mm, F.Cu at (47.5, 84.9)
- added H1: MountingHole, Mousebite:Mousebite_0.3mm, F.Cu at (44.6, 77.8)
- added H1: MountingHole, Mousebite:Mousebite_0.3mm, F.Cu at (44.6, 78.8)
- added H1: MountingHole, Mousebite:Mousebite_0.3mm, F.Cu at (-8.75, 134.4)
- added H1: MountingHole, Mousebite:Mousebite_0.3mm, F.Cu at (77.1, 85.4)
- added H1: MountingHole, Mousebite:Mousebite_0.3mm, F.Cu at (58.4, 76.3)
- added H1: MountingHole, Mousebite:Mousebite_0.3mm, F.Cu at (47.6, 77.3)
- added H1: MountingHole, Mousebite:Mousebite_0.3mm, F.Cu at (23.0, 85.3)
- added H1: MountingHole, Mousebite:Mousebite_0.3mm, F.Cu at (90.8, 77.8)
- added H1: MountingHole, Mousebite:Mousebite_0.3mm, F.Cu at (98.6, 77.3)
- added H1: MountingHole, Mousebite:Mousebite_0.3mm, F.Cu at (90.7, 93.3)
- added H1: MountingHole, Mousebite:Mousebite_0.3mm, F.Cu at (98.7, 83.4)
- added H1: MountingHole, Mousebite:Mousebite_0.3mm, F.Cu at (90.7, 84.9)
- added H1: MountingHole, Mousebite:Mousebite_0.3mm, F.Cu at (98.7, 91.8)
- added H1: MountingHole, Mousebite:Mousebite_0.3mm, F.Cu at (-16.9, 92.9)
- added H1: MountingHole, Mousebite:Mousebite_0.3mm, F.Cu at (-87.2, 127.3)
- added H1: MountingHole, Mousebite:Mousebite_0.3mm, F.Cu at (98.7, 93.3)
- added H1: MountingHole, Mousebite:Mousebite_0.3mm, F.Cu at (93.7, 79.2)
- added H1: MountingHole, Mousebite:Mousebite_0.3mm, F.Cu at (23.0, 76.3)
- added H1: MountingHole, Mousebite:Mousebite_0.3mm, F.Cu at (79.9, 93.3)
- added H1: MountingHole, Mousebite:Mousebite_0.3mm, F.Cu at (87.9, 83.4)
- added H1: MountingHole, Mousebite:Mousebite_0.3mm, F.Cu at (77.1, 91.3)
- added H1: MountingHole, Mousebite:Mousebite_0.3mm, F.Cu at (77.1, 84.4)
- added H1: MountingHole, Mousebite:Mousebite_0.3mm, F.Cu at (87.9, 85.4)
- added H1: MountingHole, Mousebite:Mousebite_0.3mm, F.Cu at (23.0, 92.2)
- added H1: MountingHole, Mousebite:Mousebite_0.3mm, F.Cu at (33.9, 82.9)
- added H1: MountingHole, Mousebite:Mousebite_0.3mm, F.Cu at (-30.3, 142.8)
- added H1: MountingHole, Mousebite:Mousebite_0.3mm, F.Cu at (33.9, 91.3)
- added H1: MountingHole, Mousebite:Mousebite_0.3mm, F.Cu at (23.0, 93.2)
- added H1: MountingHole, Mousebite:Mousebite_0.3mm, F.Cu at (23.0, 93.7)
- added H1: MountingHole, Mousebite:Mousebite_0.3mm, F.Cu at (36.7, 83.9)
- added H1: MountingHole, Mousebite:Mousebite_0.3mm, F.Cu at (44.7, 93.8)
- added H1: MountingHole, Mousebite:Mousebite_0.3mm, F.Cu at (44.7, 92.8)
- added H1: MountingHole, Mousebite:Mousebite_0.3mm, F.Cu at (33.9, 84.4)
- added H1: MountingHole, Mousebite:Mousebite_0.3mm, F.Cu at (23.0, 92.7)
- added H1: MountingHole, Mousebite:Mousebite_0.3mm, F.Cu at (25.9, 85.3)
- added H1: MountingHole, Mousebite:Mousebite_0.3mm, F.Cu at (44.7, 91.3)
- added H1: MountingHole, Mousebite:Mousebite_0.3mm, F.Cu at (-22.4, 126.8)
- added H1: MountingHole, Mousebite:Mousebite_0.3mm, F.Cu at (25.9, 92.2)
- added H1: MountingHole, Mousebite:Mousebite_0.3mm, F.Cu at (23.0, 91.2)
- added H1: MountingHole, Mousebite:Mousebite_0.3mm, F.Cu at (44.7, 84.4)
- added H1: MountingHole, Mousebite:Mousebite_0.3mm, F.Cu at (36.7, 82.9)
- added H1: MountingHole, Mousebite:Mousebite_0.3mm, F.Cu at (36.7, 83.4)
- added H1: MountingHole, Mousebite:Mousebite_0.3mm, F.Cu at (23.0, 83.3)
- added H1: MountingHole, Mousebite:Mousebite_0.3mm, F.Cu at (36.7, 91.8)
- added H1: MountingHole, Mousebite:Mousebite_0.3mm, F.Cu at (25.9, 92.7)
- added H1: MountingHole, Mousebite:Mousebite_0.3mm, F.Cu at (25.9, 84.3)
- added H1: MountingHole, Mousebite:Mousebite_0.3mm, F.Cu at (25.9, 91.7)
- added H1: MountingHole, Mousebite:Mousebite_0.3mm, F.Cu at (-30.2, 125.8)
- added H1: MountingHole, Mousebite:Mousebite_0.3mm, F.Cu at (44.7, 84.9)
- added H1: MountingHole, Mousebite:Mousebite_0.3mm, F.Cu at (33.8, 77.3)
- added H1: MountingHole, Mousebite:Mousebite_0.3mm, F.Cu at (36.7, 85.4)
- added H1: MountingHole, Mousebite:Mousebite_0.3mm, F.Cu at (33.9, 83.4)
- added H1: MountingHole, Mousebite:Mousebite_0.3mm, F.Cu at (23.0, 91.7)
- added H1: MountingHole, Mousebite:Mousebite_0.3mm, F.Cu at (33.9, 85.4)
- added H1: MountingHole, Mousebite:Mousebite_0.3mm, F.Cu at (36.7, 93.8)
- added H1: MountingHole, Mousebite:Mousebite_0.3mm, F.Cu at (33.9, 92.8)
- added H1: MountingHole, Mousebite:Mousebite_0.3mm, F.Cu at (28.9, 79.2)
- added H1: MountingHole, Mousebite:Mousebite_0.3mm, F.Cu at (33.9, 93.3)
- added H1: MountingHole, Mousebite:Mousebite_0.3mm, F.Cu at (-51.8, 127.3)
- added H1: MountingHole, Mousebite:Mousebite_0.3mm, F.Cu at (36.7, 91.3)
- added H1: MountingHole, Mousebite:Mousebite_0.3mm, F.Cu at (36.7, 92.3)
- added H1: MountingHole, Mousebite:Mousebite_0.3mm, F.Cu at (36.7, 84.4)
- added H1: MountingHole, Mousebite:Mousebite_0.3mm, F.Cu at (44.7, 85.4)
- added H1: MountingHole, Mousebite:Mousebite_0.3mm, F.Cu at (25.9, 83.3)
- added H1: MountingHole, Mousebite:Mousebite_0.3mm, F.Cu at (77.0, 78.3)
- added H1: MountingHole, Mousebite:Mousebite_0.3mm, F.Cu at (77.0, 76.3)
- added H1: MountingHole, Mousebite:Mousebite_0.3mm, F.Cu at (109.5, 91.3)
- added H1: MountingHole, Mousebite:Mousebite_0.3mm, F.Cu at (109.5, 84.4)
- added H1: MountingHole, Mousebite:Mousebite_0.3mm, F.Cu at (101.5, 82.9)
- added H1: MountingHole, Mousebite:Mousebite_0.3mm, F.Cu at (-51.8, 127.8)
- added H1: MountingHole, Mousebite:Mousebite_0.3mm, F.Cu at (79.9, 85.4)
- added H1: MountingHole, Mousebite:Mousebite_0.3mm, F.Cu at (79.9, 93.8)
- added H1: MountingHole, Mousebite:Mousebite_0.3mm, F.Cu at (58.3, 93.8)
- added H1: MountingHole, Mousebite:Mousebite_0.3mm, F.Cu at (55.5, 91.3)
- added H1: MountingHole, Mousebite:Mousebite_0.3mm, F.Cu at (47.6, 76.8)
- added H1: MountingHole, Mousebite:Mousebite_0.3mm, F.Cu at (47.5, 83.4)
- added H1: MountingHole, Mousebite:Mousebite_0.3mm, F.Cu at (66.3, 83.4)
- added H1: MountingHole, Mousebite:Mousebite_0.3mm, F.Cu at (66.3, 84.9)
- added H1: MountingHole, Mousebite:Mousebite_0.3mm, F.Cu at (55.5, 84.9)
- added H1: MountingHole, Mousebite:Mousebite_0.3mm, F.Cu at (79.9, 92.8)
- added H1: MountingHole, Mousebite:Mousebite_0.3mm, F.Cu at (-84.3, 132.4)
- added H1: MountingHole, Mousebite:Mousebite_0.3mm, F.Cu at (77.0, 78.8)
- added H1: MountingHole, Mousebite:Mousebite_0.3mm, F.Cu at (80.0, 78.8)
- added H1: MountingHole, Mousebite:Mousebite_0.3mm, F.Cu at (80.0, 78.3)
- added H1: MountingHole, Mousebite:Mousebite_0.3mm, F.Cu at (80.0, 77.3)
- added H1: MountingHole, Mousebite:Mousebite_0.3mm, F.Cu at (80.0, 77.8)
- added H1: MountingHole, Mousebite:Mousebite_0.3mm, F.Cu at (87.8, 77.3)
- added H1: MountingHole, Mousebite:Mousebite_0.3mm, F.Cu at (55.4, 78.8)
- added H1: MountingHole, Mousebite:Mousebite_0.3mm, F.Cu at (55.4, 77.8)
- added H1: MountingHole, Mousebite:Mousebite_0.3mm, F.Cu at (66.3, 92.8)
- added H1: MountingHole, Mousebite:Mousebite_0.3mm, F.Cu at (77.1, 92.3)
- added H1: MountingHole, Mousebite:Mousebite_0.3mm, F.Cu at (-84.3, 131.9)
- added H1: MountingHole, Mousebite:Mousebite_0.3mm, F.Cu at (69.1, 92.8)
- added H1: MountingHole, Mousebite:Mousebite_0.3mm, F.Cu at (26.0, 78.3)
- added H1: MountingHole, Mousebite:Mousebite_0.3mm, F.Cu at (26.0, 77.8)
- added H1: MountingHole, Mousebite:Mousebite_0.3mm, F.Cu at (58.4, 78.3)
- added H1: MountingHole, Mousebite:Mousebite_0.3mm, F.Cu at (58.3, 83.9)
- added H1: MountingHole, Mousebite:Mousebite_0.3mm, F.Cu at (26.0, 76.8)
- added H1: MountingHole, Mousebite:Mousebite_0.3mm, F.Cu at (26.0, 77.3)
- added H1: MountingHole, Mousebite:Mousebite_0.3mm, F.Cu at (26.0, 76.3)
- added H1: MountingHole, Mousebite:Mousebite_0.3mm, F.Cu at (112.2, 91.8)
- added H1: MountingHole, Mousebite:Mousebite_0.3mm, F.Cu at (112.2, 83.9)
- added H1: MountingHole, Mousebite:Mousebite_0.3mm, F.Cu at (-33.1, 133.9)
- added H1: MountingHole, Mousebite:Mousebite_0.3mm, F.Cu at (112.2, 93.8)
- added H1: MountingHole, Mousebite:Mousebite_0.3mm, F.Cu at (112.2, 85.4)
- added H1: MountingHole, Mousebite:Mousebite_0.3mm, F.Cu at (55.4, 77.3)
- added H1: MountingHole, Mousebite:Mousebite_0.3mm, F.Cu at (66.3, 85.4)
- added H1: MountingHole, Mousebite:Mousebite_0.3mm, F.Cu at (79.9, 92.3)
- added H1: MountingHole, Mousebite:Mousebite_0.3mm, F.Cu at (79.9, 84.4)
- added H1: MountingHole, Mousebite:Mousebite_0.3mm, F.Cu at (47.5, 92.8)
- added H1: MountingHole, Mousebite:Mousebite_0.3mm, F.Cu at (69.1, 93.3)
- added H1: MountingHole, Mousebite:Mousebite_0.3mm, F.Cu at (33.9, 92.3)
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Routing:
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- added copper zone on B.Cu, net (none)
- added copper zone on F.Cu, net (none)
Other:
- board size 7.8 x 17.9 mm -> 213 x 114 mm
- board text added: "RevA"
- board text added: "VCC3V3_SYS buck/boost dropin replacement"
